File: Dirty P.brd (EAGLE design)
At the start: 84.4 x 73.3 mm, 23 parts, among them J1 NMJ6HCD2, J2 NMJ6HCD2, SW1 FOOT_SW, U1 MMBT3906, U2 MMBT3906, U3 MMBT3906

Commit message: switched to 4MM caps for 10uF
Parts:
- C1, C6: device MF_Passives:CP6.3MM -> MF_Passives:CP4MM
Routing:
- net N$14: track 46.8 -> 45.7 mm
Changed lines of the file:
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@@
 <?xml version="1.0" encoding="utf-8"?>
 <!DOCTYPE eagle SYSTEM "eagle.dtd">
-<eagle version="6.6.0">
+<eagle version="6.5.0">
 <drawing>
 <settings>
@@
 <elements>
 <element name="J1" library="PP_Connectors" package="NMJ6HCD2" value="NMJ6HCD2" x="0" y="62.23" rot="R180"/>
-<element name="C1" library="MF_Passives" package="CP6.3MM" value="10uF" x="77.724" y="29.464" smashed="yes" rot="R90">
+<element name="C1" library="MF_Passives" package="CP4MM" value="10uF" x="77.724" y="29.464" smashed="yes" rot="R90">
 <attribute name="TOLERANCE" value="N/A" x="176.784" y="73.914" size="1.778" layer="27" rot="R90" display="off"/>
 <attribute name="MFG#" value="N/A" x="176.784" y="73.914" size="1.778" layer="27" rot="R90" display="off"/>
-<attribute name="VOTLAGE" value="N/A" x="176.784" y="73.914" size="1.778" layer="27" rot="R90" display="off"/>
 <attribute name="NAME" x="74.424" y="25.066" size="0.8128" layer="25" font="vector" ratio="16"/>
+<attribute name="VOLTAGE" value="N/A" x="77.724" y="29.464" size="1.778" layer="27" rot="R90" display="off"/>
 </element>
 <element name="C2" library="MF_Passives" package="C0805" value="0.1uF" x="80.772" y="34.544" smashed="yes" rot="R180">
@@
 <element name="BATT1" library="PP_Connectors" package="12BH611-GR" value="12BH611-GR" x="1.524" y="47.752"/>
 <element name="LEVEL" library="PP_Electromechanical" package="PTD901" value="PTD901-2015K-A104" x="32.766" y="67.056" rot="R180"/>
-<element name="C6" library="MF_Passives" package="CP6.3MM" value="10uF" x="51.562" y="59.182" smashed="yes">
+<element name="C6" library="MF_Passives" package="CP4MM" value="10uF" x="51.562" y="59.182" smashed="yes">
 <attribute name="TOLERANCE" value="N/A" x="103.632" y="-39.878" size="1.778" layer="27" display="off"/>
 <attribute name="MFG#" value="N/A" x="103.632" y="-39.878" size="1.778" layer="27" display="off"/>
-<attribute name="VOTLAGE" value="N/A" x="103.632" y="-39.878" size="1.778" layer="27" display="off"/>
 <attribute name="NAME" x="46.484" y="61.642" size="0.8128" layer="25" font="vector" ratio="16"/>
+<attribute name="VOLTAGE" value="N/A" x="51.562" y="59.182" size="1.778" layer="27" display="off"/>
 </element>
 <element name="SW1" library="PP_Electromechanical" package="FOOT_SW" value="FOOT_SW" x="42.1767" y="0" smashed="yes">
@@
 <via x="61.468" y="17.526" extent="1-16" drill="0.6" shape="square"/>
 <via x="49.276" y="57.15" extent="1-16" drill="0.6" shape="square"/>
-<wire x1="51.562" y1="56.482" x2="51.562" y2="57.15" width="0.4064" layer="1"/>
+<wire x1="51.562" y1="57.432" x2="51.562" y2="57.15" width="0.4064" layer="1"/>
 <wire x1="51.562" y1="57.15" x2="49.276" y2="57.15" width="0.4064" layer="1"/>
 <contactref element="ATTACK" pad="P$3"/>
@@
 <contactref element="R1" pad="P$1"/>
 <contactref element="U1" pad="P$1"/>
-<wire x1="75.024" y1="29.464" x2="75.504" y2="29.464" width="0.4064" layer="1"/>
+<wire x1="75.974" y1="29.464" x2="75.504" y2="29.464" width="0.4064" layer="1"/>
 <wire x1="75.504" y1="29.464" x2="75.504" y2="34.544" width="0.4064" layer="1"/>
 <wire x1="69.834" y1="26.99" x2="73.26265625" y2="26.99" width="0.4064" layer="1"/>
 <wire x1="73.26265625" y1="26.99" x2="75.024" y2="28.75134375" width="0.4064" layer="1" curve="90"/>
-<wire x1="75.024" y1="28.75134375" x2="75.024" y2="29.464" width="0.4064" layer="1"/>
+<wire x1="75.024" y1="28.75134375" x2="75.974" y2="29.464" width="0.4064" layer="1"/>
 </signal>
 <signal name="N$2">
@@
 <signal name="N$9">
 <contactref element="C6" pad="P$2"/>
-<wire x1="51.562" y1="61.14" x2="51.562" y2="61.882" width="0.4064" layer="1"/>
+<wire x1="51.562" y1="61.14" x2="51.562" y2="60.932" width="0.4064" layer="1"/>
 <contactref element="ATTACK" pad="P$2"/>
-<wire x1="51.562" y1="61.882" x2="51.562" y2="67.0306" width="0.4064" layer="1"/>
+<wire x1="51.562" y1="60.932" x2="51.562" y2="67.0306" width="0.4064" layer="1"/>
 <wire x1="51.562" y1="67.0306" x2="51.5874" y2="67.056" width="0.4064" layer="1" curve="-90"/>
 </signal>
@@
 <contactref element="C1" pad="P$1"/>
 <contactref element="C2" pad="P$1"/>
-<wire x1="81.722" y1="34.544" x2="81.722" y2="29.906" width="0.4064" layer="1"/>
-<wire x1="81.722" y1="29.906" x2="81.28" y2="29.464" width="0.4064" layer="1"/>
-<wire x1="81.28" y1="29.464" x2="80.424" y2="29.464" width="0.4064" layer="1"/>
+<wire x1="81.722" y1="34.544" x2="81.722" y2="30.54129375" width="0.4064" layer="1"/>
+<wire x1="81.722" y1="30.54129375" x2="80.64470625" y2="29.464" width="0.4064" layer="1" curve="-90"/>
+<wire x1="80.64470625" y1="29.464" x2="79.474" y2="29.464" width="0.4064" layer="1"/>
 <contactref element="SW1" pad="1"/>
 <wire x1="52.3367" y1="6.858" x2="52.5907" y2="6.604" width="0.4064" layer="16"/>
 <wire x1="52.5907" y1="6.604" x2="57.15" y2="6.604" width="0.4064" layer="16"/>
 <via x="57.15" y="6.604" extent="1-16" drill="0.6" shape="square"/>
-<wire x1="57.15" y1="6.604" x2="62.731796875" y2="6.604" width="0.4064" layer="1"/>
-<wire x1="62.731796875" y1="6.604" x2="80.424" y2="24.296203125" width="0.4064" layer="1" curve="90"/>
-<wire x1="80.424" y1="24.296203125" x2="80.424" y2="29.464" width="0.4064" layer="1"/>
+<wire x1="57.15" y1="6.604" x2="61.969796875" y2="6.604" width="0.4064" layer="1"/>
+<wire x1="61.969796875" y1="6.604" x2="79.662" y2="27.852203125" width="0.4064" layer="1" curve="90"/>
+<wire x1="79.662" y1="27.852203125" x2="79.474" y2="29.464" width="0.4064" layer="1"/>
 </signal>
 </signals>

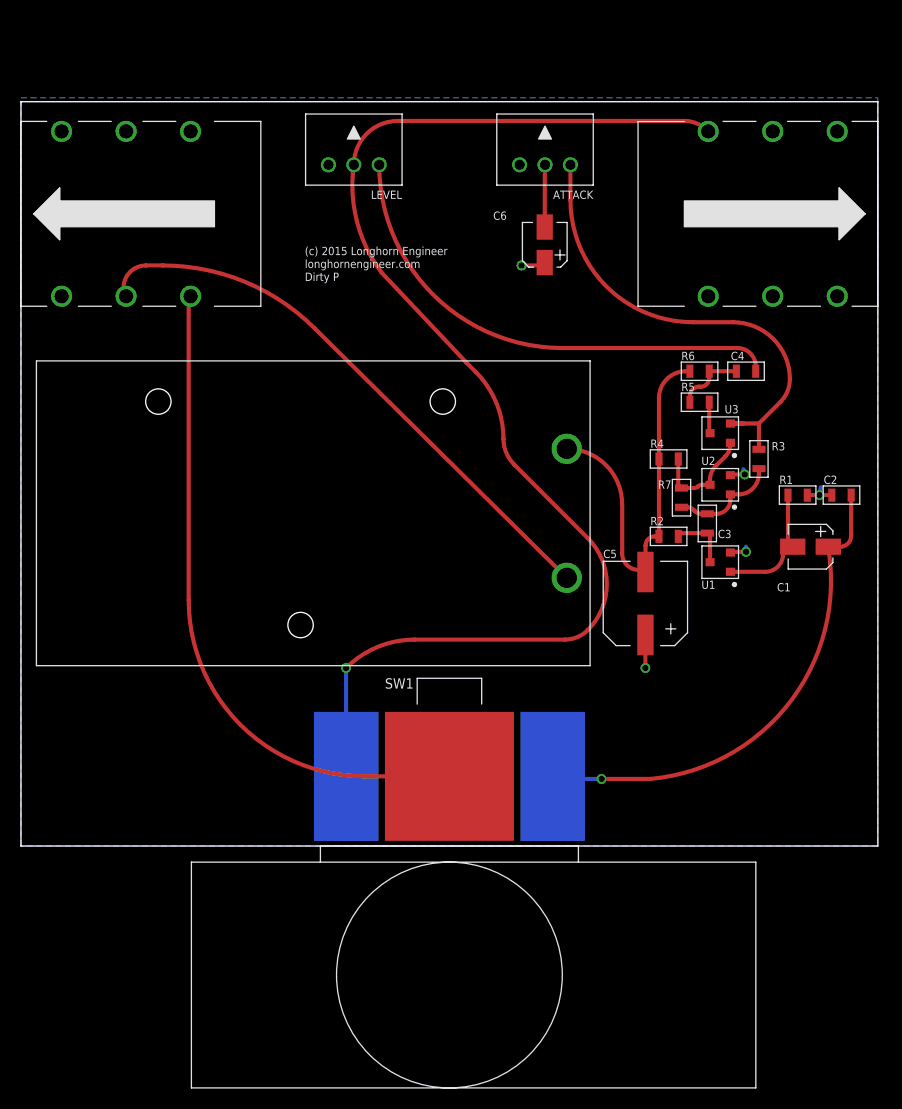
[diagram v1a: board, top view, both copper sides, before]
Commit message: REV2: Bass switch. Bias Pot added. Fixed connectors. Added space for Bosses.
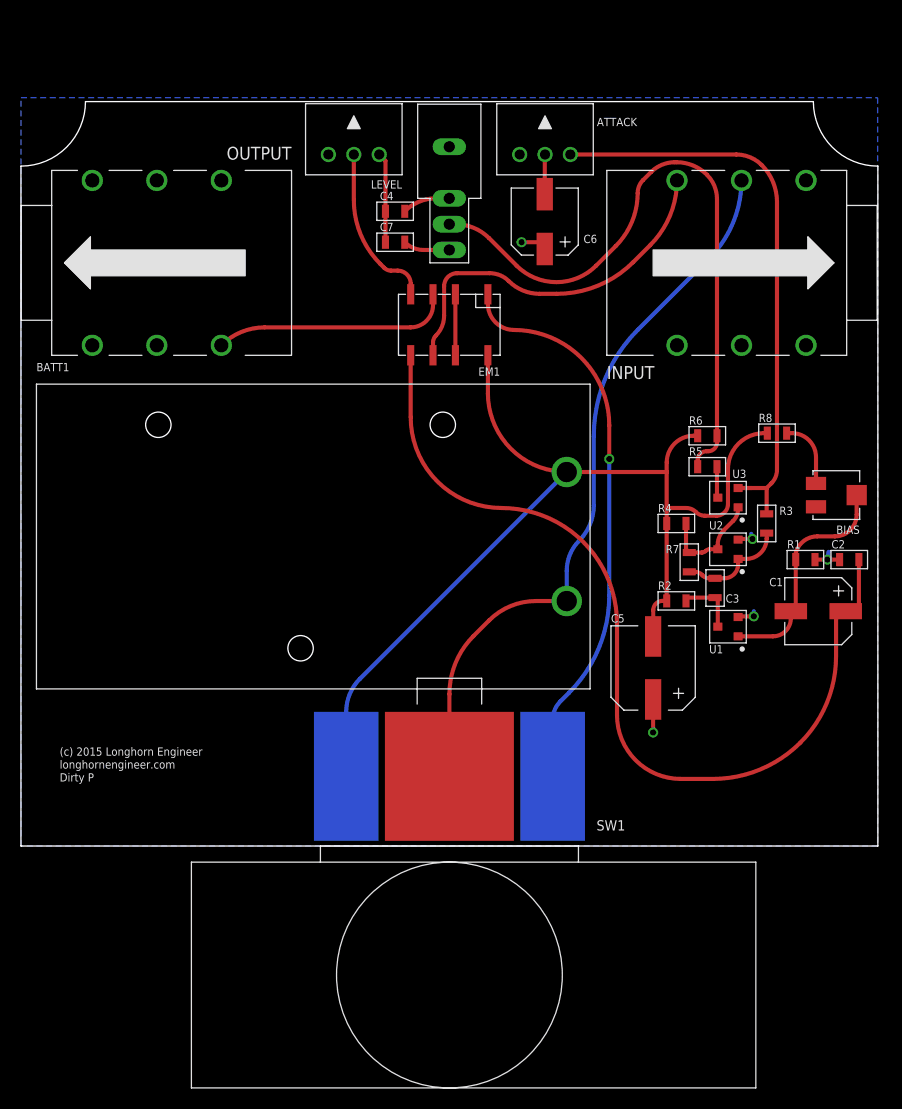
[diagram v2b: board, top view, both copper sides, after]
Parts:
- removed J1, J2: NMJ6HCD2, PP_Connectors:NMJ6HCD2
- added BIAS: 3224J-1-503E, PP_Passives:3224J
- added C7: 0.005uF, MF_Passives:C0805
- added EM1: 6-1462037-4, PP_Electromechanical:IM_RELAY
- added INPUT, OUTPUT: NMJ6HCD2, PP_Connectors:NMJ6HCD2
- added R8: 100K, MF_Passives:R0805
- added SW2: ET01MD1AVBE, PP_Electromechanical:ET03MD1AVBE
- C1, C6: value 10uF -> RSS1E100MCN1GS; device MF_Passives:CP4MM -> MF_Passives:CP6.3MM
- C5: value 50uF -> RPS1H470MCN1GS
- moved U$1 54.9 mm to (3.81, 3.81)
- moved C4 38.0 mm to (36.8, 62.5)
- moved C3 6.40 mm to (68.3, 25.4)
- moved R2 6.40 mm to (64.5, 24.1)
- moved R3 6.40 mm to (73.4, 31.8)
- moved R4 6.40 mm to (64.5, 31.8)
- moved U1 6.40 mm to (69.6, 21.6)
- moved U2 6.40 mm to (69.6, 29.2)
- moved U3 6.40 mm to (69.6, 34.3)
- moved C5 6.40 mm to (62.2, 17.5)
- moved R5 6.40 mm to (67.6, 37.3)
- moved C1 6.40 mm to (78.5, 23.1)
- moved C2 6.40 mm to (81.5, 28.2)
- moved R1 6.40 mm to (77.2, 28.2)
- moved R7 6.40 mm to (65.8, 27.9)
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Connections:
- removed net N$10: J2.R
- new net N$12: BIAS.3, R8.P$2
- new net N$15: C4.P$2, SW2.P$1
- new net N$16: C7.P$2, SW2.P$3
- new net N$17: EM1.P$2, EM1.P$7
- new net N$19: EM1.P$4, LEVEL.P$2
- new net N$21: EM1.P$1, SW1.1
- net 9V: now also INPUT.R, SW1.COM; no longer J1.R
- net GND: now also INPUT.S, OUTPUT.S; no longer J1.S, J2.S
- net N$1: now also BIAS.2
- net N$11: now also EM1.P$3, OUTPUT.T; no longer J2.T, LEVEL.P$2, SW1.2
- net N$13: now also C4.P$1, C7.P$1; no longer C4.P$2
- net N$14: now also EM1.P$5; no longer SW1.1
- net N$4: now also EM1.P$8, R8.P$1, SW1.2
- net N$5: now also SW2.P$2; no longer C4.P$1
- net SIG_IN: now also EM1.P$6, INPUT.T; no longer J1.T, SW1.COM
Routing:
- net N$11: track 125.9 -> 23.2 mm, vias 1 -> 0
- net N$4: track 38.0 -> 101.1 mm
- net N$5: track 6.60 -> 62.5 mm
- net N$21: track 0.00 -> 53.7 mm, vias 0 -> 1
- net N$14: track 45.7 -> 86.1 mm, vias 1 -> 0
- net N$13: track 45.8 -> 8.89 mm
- net SIG_IN: track 62.9 -> 36.5 mm
- net N$19: track 0.00 -> 16.1 mm
- net 9V: track 56.7 -> 70.8 mm
- net N$8: track 44.5 -> 58.1 mm
- net N$1: track 12.7 -> 22.1 mm
- net N$12: track 0.00 -> 6.45 mm
- net N$17: track 0.00 -> 6.00 mm
- net N$15: track 0.00 -> 4.64 mm
- net N$16: track 0.00 -> 4.54 mm
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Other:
- outline, holes or cut-outs redrawn

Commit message: changed out switch and rerouted some stuff.
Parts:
- SW2: value ET01MD1AVBE -> 108-0020-EVX; device PP_Electromechanical:ET03MD1AVBE -> PP_Electromechanical:108-0020-EVX
- moved EM1 9.40 mm to (32.8, 51.1)
- moved SW2 4.57 mm to (42.2, 59.2)
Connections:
- net N$4: no longer SW1.2
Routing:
- net 9V: track 70.8 -> 136.8 mm
- net N$4: track 101.1 -> 72.4 mm
- net N$21: track 53.7 -> 78.3 mm
- net SIG_IN: track 36.5 -> 51.4 mm
- net N$11: track 23.2 -> 13.1 mm
- net N$14: track 86.1 -> 92.5 mm
- net N$16: track 4.54 -> 10.2 mm
- net N$8: track 58.1 -> 54.4 mm
- net N$19: track 16.1 -> 14.8 mm
- net N$15: track 4.64 -> 5.76 mm
- net N$5: track 62.5 -> 61.6 mm

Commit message: Changed caps back
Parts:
- added R9: 50K, MF_Passives:R0805
- C1, C6: value RSS1E100MCN1GS -> 10uF; device MF_Passives:CP6.3MM -> MF_Passives:CP4MM
- C5: value RPS1H470MCN1GS -> 50uF
- C7: value 0.005uF -> 0.001uF
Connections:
- new net N$10: LEVEL.P$1, R9.P$2
- net N$13: now also R9.P$1; no longer LEVEL.P$1
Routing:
- net N$10: track 0.00 -> 5.24 mm
- net N$13: track 8.89 -> 5.48 mm
- net N$14: track 92.5 -> 90.8 mm
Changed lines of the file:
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@@
 <?xml version="1.0" encoding="utf-8"?>
 <!DOCTYPE eagle SYSTEM "eagle.dtd">
-<eagle version="6.6.0">
+<eagle version="6.5.0">
 <drawing>
 <settings>
@@
 <elements>
 <element name="INPUT" library="PP_Connectors" package="NMJ6HCD2" value="NMJ6HCD2" x="81.28" y="57.404"/>
-<element name="C1" library="MF_Passives" package="CP6.3MM" value="RSS1E100MCN1GS" x="78.486" y="23.114" smashed="yes" rot="R90">
+<element name="C1" library="MF_Passives" package="CP4MM" value="10uF" x="78.486" y="23.114" smashed="yes" rot="R90">
 <attribute name="TOLERANCE" value="N/A" x="177.546" y="67.564" size="1.778" layer="27" rot="R90" display="off"/>
 <attribute name="MFG#" value="N/A" x="177.546" y="67.564" size="1.778" layer="27" rot="R90" display="off"/>
 <attribute name="NAME" x="73.662" y="25.574" size="0.8128" layer="25" font="vector" ratio="16"/>
-<attribute name="VOTLAGE" value="N/A" x="78.486" y="23.114" size="1.778" layer="27" rot="R90" display="off"/>
+<attribute name="VOLTAGE" value="N/A" x="78.486" y="23.114" size="1.778" layer="27" rot="R90" display="off"/>
 </element>
 <element name="C2" library="MF_Passives" package="C0805" value="0.1uF" x="81.534" y="28.194" smashed="yes" rot="R180">
@@
 <attribute name="TEMP_COF" value="N/A" x="77.47" y="-51.816" size="1.778" layer="27" display="off"/>
 </element>
-<element name="C5" library="MF_Passives" package="CP8MM" value="RPS1H470MCN1GS" x="62.23" y="17.526" smashed="yes">
+<element name="C5" library="MF_Passives" package="CP8MM" value="50uF" x="62.23" y="17.526" smashed="yes">
 <attribute name="TOLERANCE" value="N/A" x="97.79" y="-82.804" size="1.778" layer="27" display="off"/>
 <attribute name="MFG#" value="N/A" x="97.79" y="-82.804" size="1.778" layer="27" display="off"/>
@@
 <element name="BATT1" library="PP_Connectors" package="12BH611-GR" value="12BH611-GR" x="1.524" y="45.466"/>
 <element name="LEVEL" library="PP_Electromechanical" package="PTD901" value="PTD901-2015K-A104" x="32.766" y="68.072" rot="R180"/>
-<element name="C6" library="MF_Passives" package="CP6.3MM" value="RSS1E100MCN1GS" x="51.562" y="61.468" smashed="yes">
+<element name="C6" library="MF_Passives" package="CP4MM" value="10uF" x="51.562" y="61.468" smashed="yes">
 <attribute name="TOLERANCE" value="N/A" x="103.632" y="-37.592" size="1.778" layer="27" display="off"/>
 <attribute name="MFG#" value="N/A" x="103.632" y="-37.592" size="1.778" layer="27" display="off"/>
 <attribute name="NAME" x="55.374" y="59.356" size="0.8128" layer="25" font="vector" ratio="16"/>
-<attribute name="VOTLAGE" value="N/A" x="51.562" y="61.468" size="1.778" layer="27" display="off"/>
+<attribute name="VOLTAGE" value="N/A" x="51.562" y="61.468" size="1.778" layer="27" display="off"/>
 </element>
 <element name="SW1" library="PP_Electromechanical" package="FOOT_SW" value="FOOT_SW" x="42.1767" y="0" smashed="yes">
@@
 <element name="BIAS" library="PP_Passives" package="3224J" value="3224J-1-503E" x="80.264" y="34.544" rot="R180"/>
 <element name="SW2" library="PP_Electromechanical" package="108-0020-EVX" value="108-0020-EVX" x="42.1767" y="59.182" rot="R180"/>
-<element name="C7" library="MF_Passives" package="C0805" value="0.005uF" x="36.83" y="59.436">
+<element name="C7" library="MF_Passives" package="C0805" value="0.001uF" x="36.83" y="59.436">
 <attribute name="TOLERANCE" value="N/A" x="36.83" y="59.436" size="1.778" layer="27" display="off"/>
 <attribute name="MFG#" value="N/A" x="36.83" y="59.436" size="1.778" layer="27" display="off"/>
@@
 </element>
 <element name="EM1" library="PP_Electromechanical" package="IM_RELAY" value="6-1462037-4" x="32.766" y="51.054" rot="R180"/>
+<element name="R9" library="MF_Passives" package="R0805" value="50K" x="33.528" y="62.23" rot="R90">
+<attribute name="TOLERANCE" value="N/A" x="33.528" y="62.23" size="1.778" layer="27" rot="R90" display="off"/>
+<attribute name="MFG#" value="N/A" x="33.528" y="62.23" size="1.778" layer="27" rot="R90" display="off"/>
+<attribute name="VOLTAGE" value="N/A" x="33.528" y="62.23" size="1.778" layer="27" rot="R90" display="off"/>
+<attribute name="WATTAGE" value="N/A" x="33.528" y="62.23" size="1.778" layer="27" rot="R90" display="off"/>
+</element>
 </elements>
 <signals>
@@
 <via x="62.23" y="11.176" extent="1-16" drill="0.6" shape="square"/>
 <via x="49.276" y="59.436" extent="1-16" drill="0.6" shape="square"/>
-<wire x1="51.562" y1="58.768" x2="51.562" y2="59.436" width="0.4064" layer="1"/>
+<wire x1="51.562" y1="59.718" x2="51.562" y2="59.436" width="0.4064" layer="1"/>
 <wire x1="51.562" y1="59.436" x2="49.276" y2="59.436" width="0.4064" layer="1"/>
 <contactref element="ATTACK" pad="P$3"/>
@@
 <contactref element="R1" pad="P$1"/>
 <contactref element="U1" pad="P$1"/>
-<wire x1="75.786" y1="23.114" x2="76.266" y2="23.114" width="0.4064" layer="1"/>
+<wire x1="76.736" y1="23.114" x2="76.266" y2="23.114" width="0.4064" layer="1"/>
 <wire x1="76.266" y1="23.114" x2="76.266" y2="28.194" width="0.4064" layer="1"/>
 <wire x1="70.596" y1="20.64" x2="74.02465625" y2="20.64" width="0.4064" layer="1"/>
 <wire x1="74.02465625" y1="20.64" x2="75.786" y2="22.40134375" width="0.4064" layer="1" curve="90"/>
-<wire x1="75.786" y1="22.40134375" x2="75.786" y2="23.114" width="0.4064" layer="1"/>
+<wire x1="75.786" y1="22.40134375" x2="76.736" y2="23.114" width="0.4064" layer="1"/>
 <contactref element="BIAS" pad="2"/>
 <wire x1="82.264" y1="34.544" x2="82.264" y2="32.62024375" width="0.4064" layer="1"/>
@@
 <signal name="N$9">
 <contactref element="C6" pad="P$2"/>
-<wire x1="51.562" y1="63.426" x2="51.562" y2="64.168" width="0.4064" layer="1"/>
+<wire x1="51.562" y1="63.426" x2="51.562" y2="63.218" width="0.4064" layer="1"/>
 <contactref element="ATTACK" pad="P$2"/>
-<wire x1="51.562" y1="64.168" x2="51.562" y2="68.0466" width="0.4064" layer="1"/>
+<wire x1="51.562" y1="63.218" x2="51.562" y2="68.0466" width="0.4064" layer="1"/>
 <wire x1="51.562" y1="68.0466" x2="51.5874" y2="68.072" width="0.4064" layer="1"/>
 </signal>
 <signal name="N$13">
-<contactref element="LEVEL" pad="P$1"/>
 <contactref element="C4" pad="P$1"/>
 <contactref element="C7" pad="P$1"/>
-<wire x1="35.266" y1="68.072" x2="35.88" y2="67.458" width="0.4064" layer="1"/>
-<wire x1="35.88" y1="67.458" x2="35.88" y2="62.484" width="0.4064" layer="1"/>
-<wire x1="35.88" y1="62.484" x2="35.88" y2="59.436" width="0.4064" layer="1"/>
+<wire x1="35.88" y1="62.484" x2="35.88" y2="61.468" width="0.4064" layer="1"/>
+<contactref element="R9" pad="P$1"/>
+<wire x1="35.88" y1="61.468" x2="35.88" y2="59.436" width="0.4064" layer="1"/>
+<wire x1="33.528" y1="61.28" x2="35.692" y2="61.28" width="0.4064" layer="1"/>
+<wire x1="35.692" y1="61.28" x2="35.88" y2="61.468" width="0.4064" layer="1"/>
 </signal>
 <signal name="N$14">
 <contactref element="C1" pad="P$1"/>
 <contactref element="C2" pad="P$1"/>
-<wire x1="82.484" y1="28.194" x2="82.484" y2="23.17529375" width="0.4064" layer="1"/>
-<wire x1="82.484" y1="23.17529375" x2="81.40670625" y2="23.114" width="0.4064" layer="1" curve="-90"/>
-<wire x1="81.40670625" y1="23.114" x2="81.186" y2="23.114" width="0.4064" layer="1"/>
 <contactref element="EM1" pad="P$5"/>
 <wire x1="47.3036375" y1="33.274" x2="58.674" y2="21.9036375" width="0.4064" layer="1" curve="-90"/>
@@
 <wire x1="76.723728125" y1="10.175728125" x2="80.236" y2="18.655103125" width="0.4064" layer="1" curve="45"/>
 <wire x1="80.236" y1="18.655103125" x2="80.236" y2="23.114" width="0.4064" layer="1"/>
-<wire x1="80.236" y1="23.114" x2="81.186" y2="23.114" width="0.4064" layer="1"/>
 <wire x1="47.3036375" y1="33.274" x2="33.760071875" y2="38.883928125" width="0.4064" layer="1" curve="-45"/>
 <wire x1="33.760071875" y1="38.883928125" x2="32.0603" y2="40.5837" width="0.4064" layer="1"/>
 <wire x1="32.0603" y1="40.5837" x2="28.966" y2="48.054" width="0.4064" layer="1" curve="-45"/>
+<wire x1="82.484" y1="28.194" x2="80.481475" y2="23.359475" width="0.4064" layer="1" curve="-44.999981"/>
+<wire x1="80.481475" y1="23.359475" x2="80.236" y2="23.114" width="0.4064" layer="1"/>
 </signal>
 <signal name="N$12">
@@
 <wire x1="36.566" y1="52.344603125" x2="36.566" y2="54.054" width="0.4064" layer="1"/>
 </signal>
+<signal name="N$10">
+<contactref element="R9" pad="P$2"/>
+<contactref element="LEVEL" pad="P$1"/>
+<wire x1="35.266" y1="68.072" x2="35.266" y2="67.375903125" width="0.4064" layer="1"/>
+<wire x1="35.266" y1="67.375903125" x2="33.528" y2="63.18" width="0.4064" layer="1" curve="-45"/>
+</signal>
 </signals>

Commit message: changed R9 to 51K cause 50K doesnt really exist
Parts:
- R9: value 50K -> 51K
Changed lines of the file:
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@@
 </element>
 <element name="EM1" library="PP_Electromechanical" package="IM_RELAY" value="6-1462037-4" x="32.766" y="51.054" rot="R180"/>
-<element name="R9" library="MF_Passives" package="R0805" value="50K" x="33.528" y="62.23" rot="R90">
+<element name="R9" library="MF_Passives" package="R0805" value="51K" x="33.528" y="62.23" rot="R90">
 <attribute name="TOLERANCE" value="N/A" x="33.528" y="62.23" size="1.778" layer="27" rot="R90" display="off"/>
 <attribute name="MFG#" value="N/A" x="33.528" y="62.23" size="1.778" layer="27" rot="R90" display="off"/>
